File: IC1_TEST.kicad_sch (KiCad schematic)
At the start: 26 parts, among them IC1 ADM3054WBRWZ-RL7-!my_lib, J1 B4B-XH-A_LF__SN_-!my_lib, SW1 SW_DIP_x03, SW2 SW_Push, U1 DEV-16771, U2 MAX6369KA+T

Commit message: pcb changes
changed connectors, redid wire paths
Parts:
- J1: footprint Connector_Molex:Molex_CLIK-Mate_502382-0470_1x04-1MP_P1.25mm_Vertical -> Connector_Molex:Molex_SL_171971-0004_1x04_P2.54mm_Vertical
- SBUS_CONN1, wheel_speed_sensor1, wheel_speed_sensor2: footprint Connector_Molex:Molex_CLIK-Mate_502382-0370_1x03-1MP_P1.25mm_Vertical -> Connector_Molex:Molex_SL_171971-0003_1x03_P2.54mm_Vertical
- WATCHDOG_RELAY_COILS1: footprint Connector_Molex:Molex_CLIK-Mate_502382-0270_1x02-1MP_P1.25mm_Vertical -> Connector_Molex:Molex_SL_171971-0002_1x02_P2.54mm_Vertical
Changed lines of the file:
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@@
       (effects (font (size 1.27 1.27)) (justify left))
     )
-    (property "Footprint" "Connector_Molex:Molex_CLIK-Mate_502382-0470_1x04-1MP_P1.25mm_Vertical" (id 2) (at 133.35 142.24 0)
+    (property "Footprint" "Connector_Molex:Molex_SL_171971-0004_1x04_P2.54mm_Vertical" (id 2) (at 133.35 142.24 0)
       (effects (font (size 1.27 1.27)) (justify left) hide)
     )
@@
       (effects (font (size 1.27 1.27)) (justify left))
     )
-    (property "Footprint" "Connector_Molex:Molex_CLIK-Mate_502382-0370_1x03-1MP_P1.25mm_Vertical" (id 2) (at 162.56 53.34 0)
+    (property "Footprint" "Connector_Molex:Molex_SL_171971-0003_1x03_P2.54mm_Vertical" (id 2) (at 162.56 53.34 0)
       (effects (font (size 1.27 1.27)) hide)
     )
@@
       (effects (font (size 1.27 1.27)) (justify left))
     )
-    (property "Footprint" "Connector_Molex:Molex_CLIK-Mate_502382-0370_1x03-1MP_P1.25mm_Vertical" (id 2) (at 163.83 66.04 0)
+    (property "Footprint" "Connector_Molex:Molex_SL_171971-0003_1x03_P2.54mm_Vertical" (id 2) (at 163.83 66.04 0)
       (effects (font (size 1.27 1.27)) hide)
     )
@@
       (effects (font (size 1.27 1.27)) (justify left))
     )
-    (property "Footprint" "Connector_Molex:Molex_CLIK-Mate_502382-0270_1x02-1MP_P1.25mm_Vertical" (id 2) (at 187.96 78.74 0)
+    (property "Footprint" "Connector_Molex:Molex_SL_171971-0002_1x02_P2.54mm_Vertical" (id 2) (at 187.96 78.74 0)
       (effects (font (size 1.27 1.27)) hide)
     )
@@
       (effects (font (size 1.27 1.27)) (justify left))
     )
-    (property "Footprint" "Connector_Molex:Molex_CLIK-Mate_502382-0370_1x03-1MP_P1.25mm_Vertical" (id 2) (at 209.55 71.12 0)
+    (property "Footprint" "Connector_Molex:Molex_SL_171971-0003_1x03_P2.54mm_Vertical" (id 2) (at 209.55 71.12 0)
       (effects (font (size 1.27 1.27)) hide)
     )
@@
     )
     (path "/00000000-0000-0000-0000-00006216a189"
-      (reference "J1") (unit 1) (value "B4B-XH-A_LF__SN_-!my_lib") (footprint "Connector_Molex:Molex_CLIK-Mate_502382-0470_1x04-1MP_P1.25mm_Vertical")
+      (reference "J1") (unit 1) (value "B4B-XH-A_LF__SN_-!my_lib") (footprint "Connector_Molex:Molex_SL_171971-0004_1x04_P2.54mm_Vertical")
     )
     (path "/00000000-0000-0000-0000-00006216d761"
@@
     )
     (path "/00000000-0000-0000-0000-0000621a4fe9"
-      (reference "SBUS_CONN1") (unit 1) (value "Conn_01x03_Female") (footprint "Connector_Molex:Molex_CLIK-Mate_502382-0370_1x03-1MP_P1.25mm_Vertical")
+      (reference "SBUS_CONN1") (unit 1) (value "Conn_01x03_Female") (footprint "Connector_Molex:Molex_SL_171971-0003_1x03_P2.54mm_Vertical")
     )
     (path "/00000000-0000-0000-0000-00006218db89"
@@
     )
     (path "/00000000-0000-0000-0000-000062193cc5"
-      (reference "WATCHDOG_RELAY_COILS1") (unit 1) (value "Conn_01x02_Female") (footprint "Connector_Molex:Molex_CLIK-Mate_502382-0270_1x02-1MP_P1.25mm_Vertical")
+      (reference "WATCHDOG_RELAY_COILS1") (unit 1) (value "Conn_01x02_Female") (footprint "Connector_Molex:Molex_SL_171971-0002_1x02_P2.54mm_Vertical")
     )
     (path "/346311ef-7b1f-4644-ae2b-5cf442f28312"
@@
     )
     (path "/00000000-0000-0000-0000-0000621879a2"
-      (reference "wheel_speed_sensor1") (unit 1) (value "Conn_01x03_Female") (footprint "Connector_Molex:Molex_CLIK-Mate_502382-0370_1x03-1MP_P1.25mm_Vertical")
+      (reference "wheel_speed_sensor1") (unit 1) (value "Conn_01x03_Female") (footprint "Connector_Molex:Molex_SL_171971-0003_1x03_P2.54mm_Vertical")
     )
     (path "/00000000-0000-0000-0000-000062188d06"
-      (reference "wheel_speed_sensor2") (unit 1) (value "Conn_01x03_Female") (footprint "Connector_Molex:Molex_CLIK-Mate_502382-0370_1x03-1MP_P1.25mm_Vertical")
-    )
-  )
+      (reference "wheel_speed_sensor2") (unit 1) (value "Conn_01x03_Female") (footprint "Connector_Molex:Molex_SL_171971-0003_1x03_P2.54mm_Vertical")
+    )
+  )

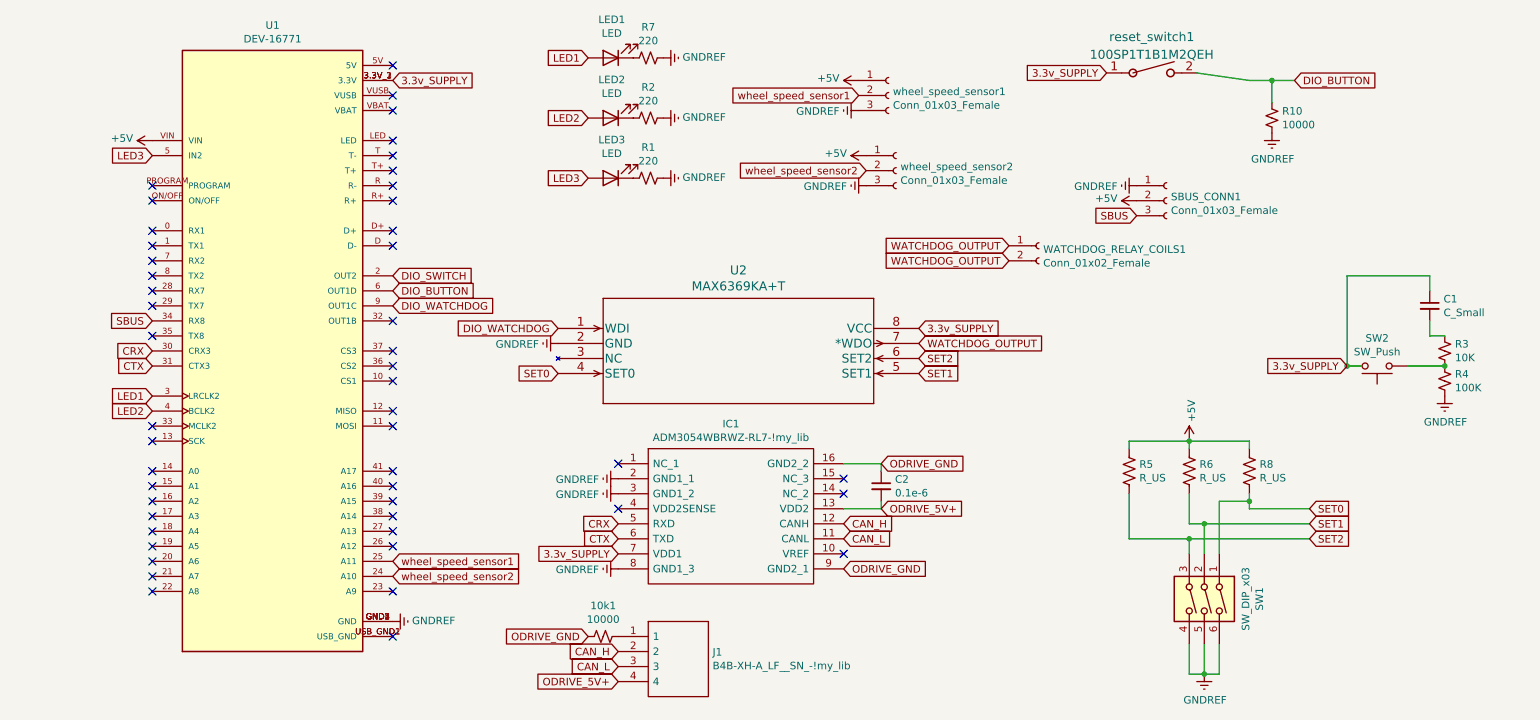
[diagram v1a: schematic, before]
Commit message: no more overlapping w/ pads, finished teensy pins
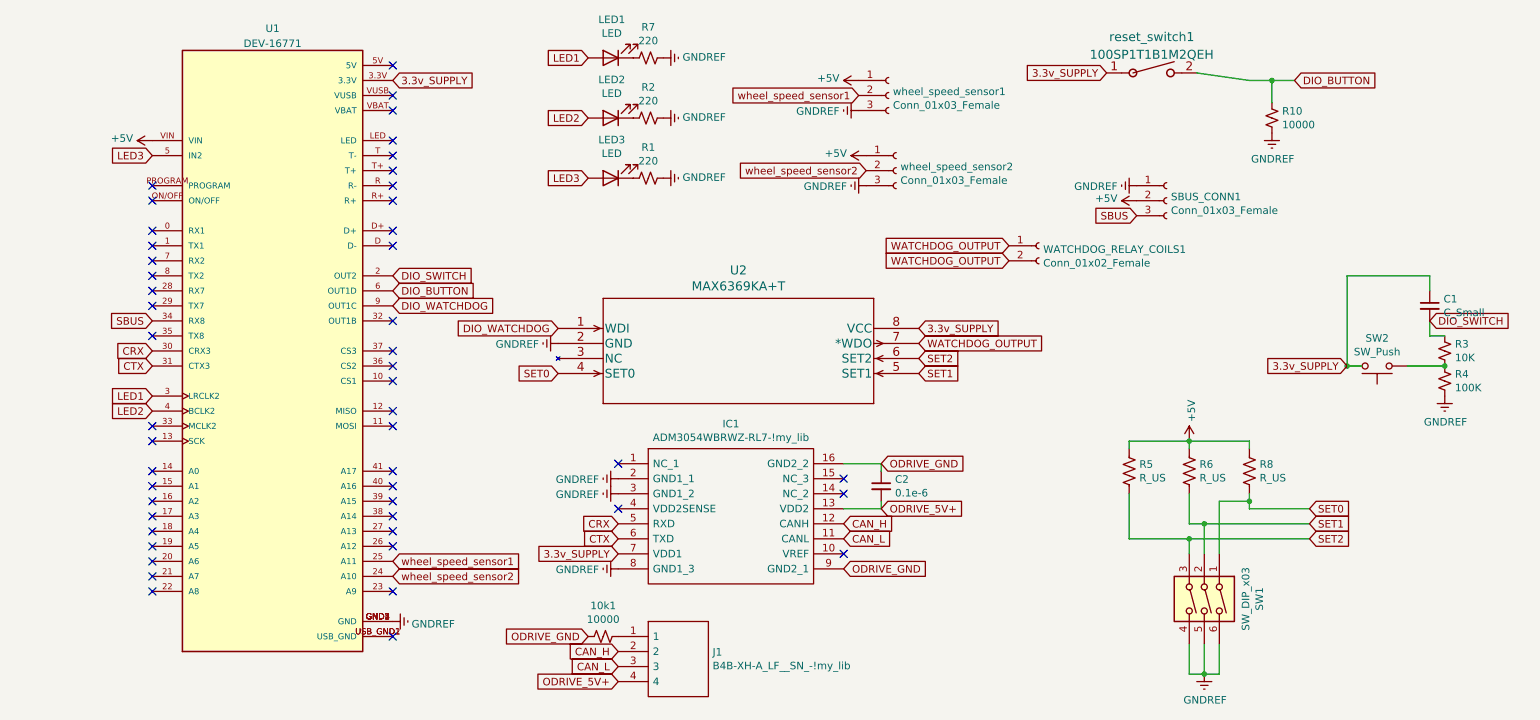
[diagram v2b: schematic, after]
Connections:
- net 3.3v_SUPPLY: now also U1.3.3V; no longer U1.3.3V_1 (3.3V), U1.3.3V_2 (3.3V), U1.3.3V_3 (3.3V)
- net DIO_SWITCH: now also C1.2, R3.1

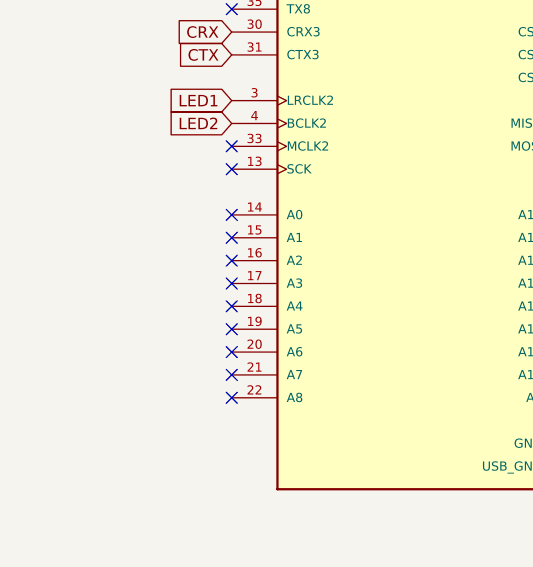
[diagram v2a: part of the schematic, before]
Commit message: added watchdog output connection to teensy
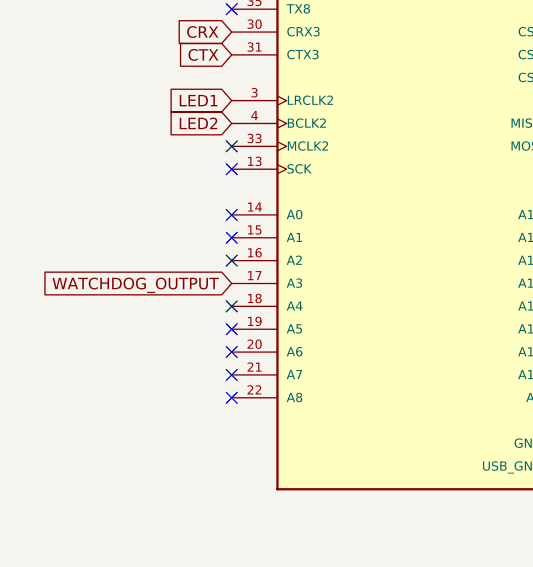
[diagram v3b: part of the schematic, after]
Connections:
- net WATCHDOG_OUTPUT: now also U1.17 (A3)
- no-connect marks 49 -> 48
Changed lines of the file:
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@@
   (no_connect (at 38.1 129.54))
   (no_connect (at 38.1 127))
-  (no_connect (at 38.1 124.46))
   (no_connect (at 116.84 123.19))
   (no_connect (at 116.84 115.57))
@@
   (no_connect (at 78.74 124.46))
   (no_connect (at 78.74 127))
+  (no_connect (at 38.1 68.58))
   (no_connect (at 38.1 78.74))
   (no_connect (at 38.1 76.2))
   (no_connect (at 38.1 71.12))
-  (no_connect (at 38.1 68.58))
   (no_connect (at 154.94 120.65))
   (wire (pts (xy 213.36 111.76) (xy 213.36 113.03))
@@
     (property "Intersheet References" "${INTERSHEET_REFS}" (id 0) (at 0 0 0)
       (effects (font (size 1.27 1.27)) hide)
+    )
+  )
+  (global_label "WATCHDOG_OUTPUT" (shape input) (at 38.1 124.46 180) (fields_autoplaced)
+    (effects (font (size 1.27 1.27)) (justify right))
+    (property "Intersheet References" "${INTERSHEET_REFS}" (id 0) (at 17.544 124.3806 0)
+      (effects (font (size 1.27 1.27)) (justify right) hide)
     )
   )
@@
   (symbol (lib_id "power:GNDREF") (at 78.74 142.24 90) (unit 1)
     (in_bom yes) (on_board yes) (fields_autoplaced)
-    (property "Reference" "#PWR?" (id 0) (at 85.09 142.24 0)
+    (property "Reference" "#PWR0101" (id 0) (at 85.09 142.24 0)
       (effects (font (size 1.27 1.27)) hide)
     )
@@
       (reference "#PWR01") (unit 1) (value "GNDREF") (footprint "")
     )
+    (path "/88d23e0a-a25b-4026-a2e3-f92f8f492ad4"
+      (reference "#PWR0101") (unit 1) (value "GNDREF") (footprint "")
+    )
     (path "/00000000-0000-0000-0000-0000621714f0"
       (reference "#PWR0102") (unit 1) (value "GNDREF") (footprint "")
@@
       (reference "#PWR0118") (unit 1) (value "GNDREF") (footprint "")
     )
-    (path "/88d23e0a-a25b-4026-a2e3-f92f8f492ad4"
-      (reference "#PWR?") (unit 1) (value "GNDREF") (footprint "")
-    )
     (path "/00000000-0000-0000-0000-00006217773d"
